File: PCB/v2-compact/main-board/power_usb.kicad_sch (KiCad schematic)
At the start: 0 parts

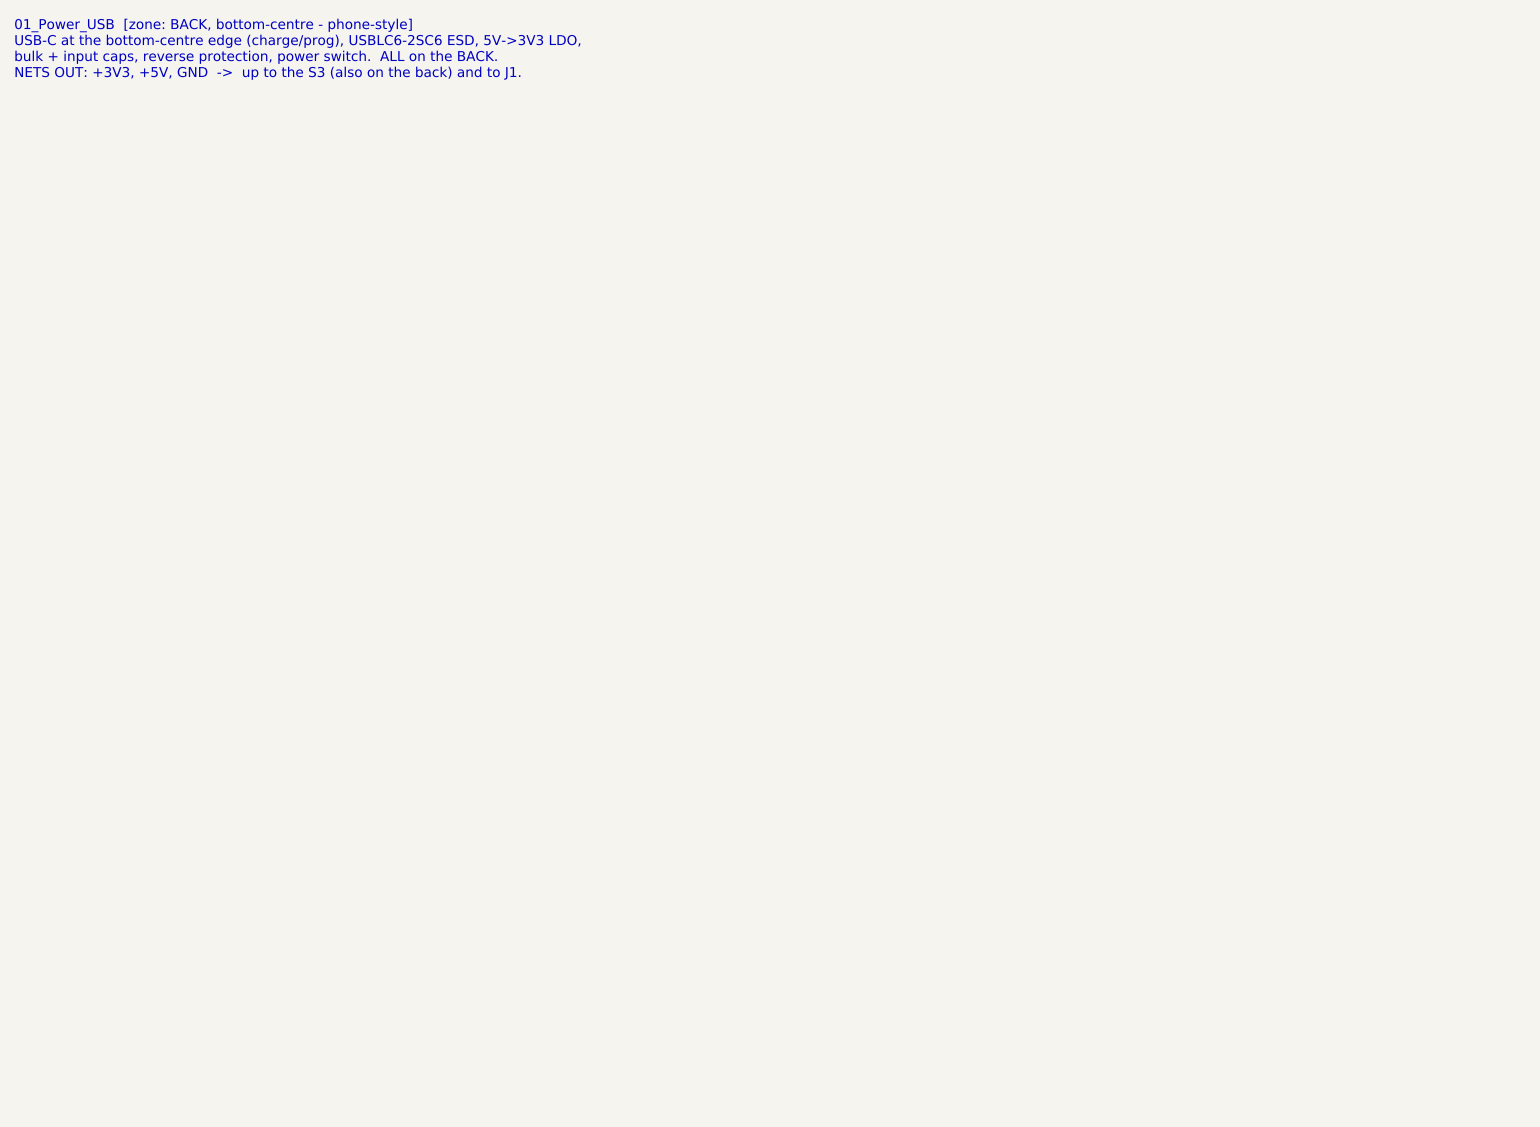
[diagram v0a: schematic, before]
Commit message: Schematics: capture PN532, GPS, IR, and both power sheets
- 07_NFC_PN532: I2C mode (I0/I1 set), 27.12MHz crystal, VMID cap, internal
  DVDD/SVDD regulator outputs correctly decoupled (not tied to 3V3), pull-ups;
  antenna pins flagged for the RF matching pass.
- 10_GPS: NEO-M9N UART to the C5, power + decoupling; bias-tee/antenna flagged.
- 11_IR: TSOP receiver + IR-LED transmitter (NPN driver).
- 02_Power (shield): local AP7361C LDO for the C5 rail + bulk caps + PWR_FLAGs.
- 01_Power_USB (main): USB-C, CC resistors, USBLC6 ESD, AP7361C 3V3 LDO.

All netlist-verified. Remaining ERC items are expected WIP (no-connects on unused
IC pins + power flags), to be cleaned once the MCU sheets tie in the shared nets.
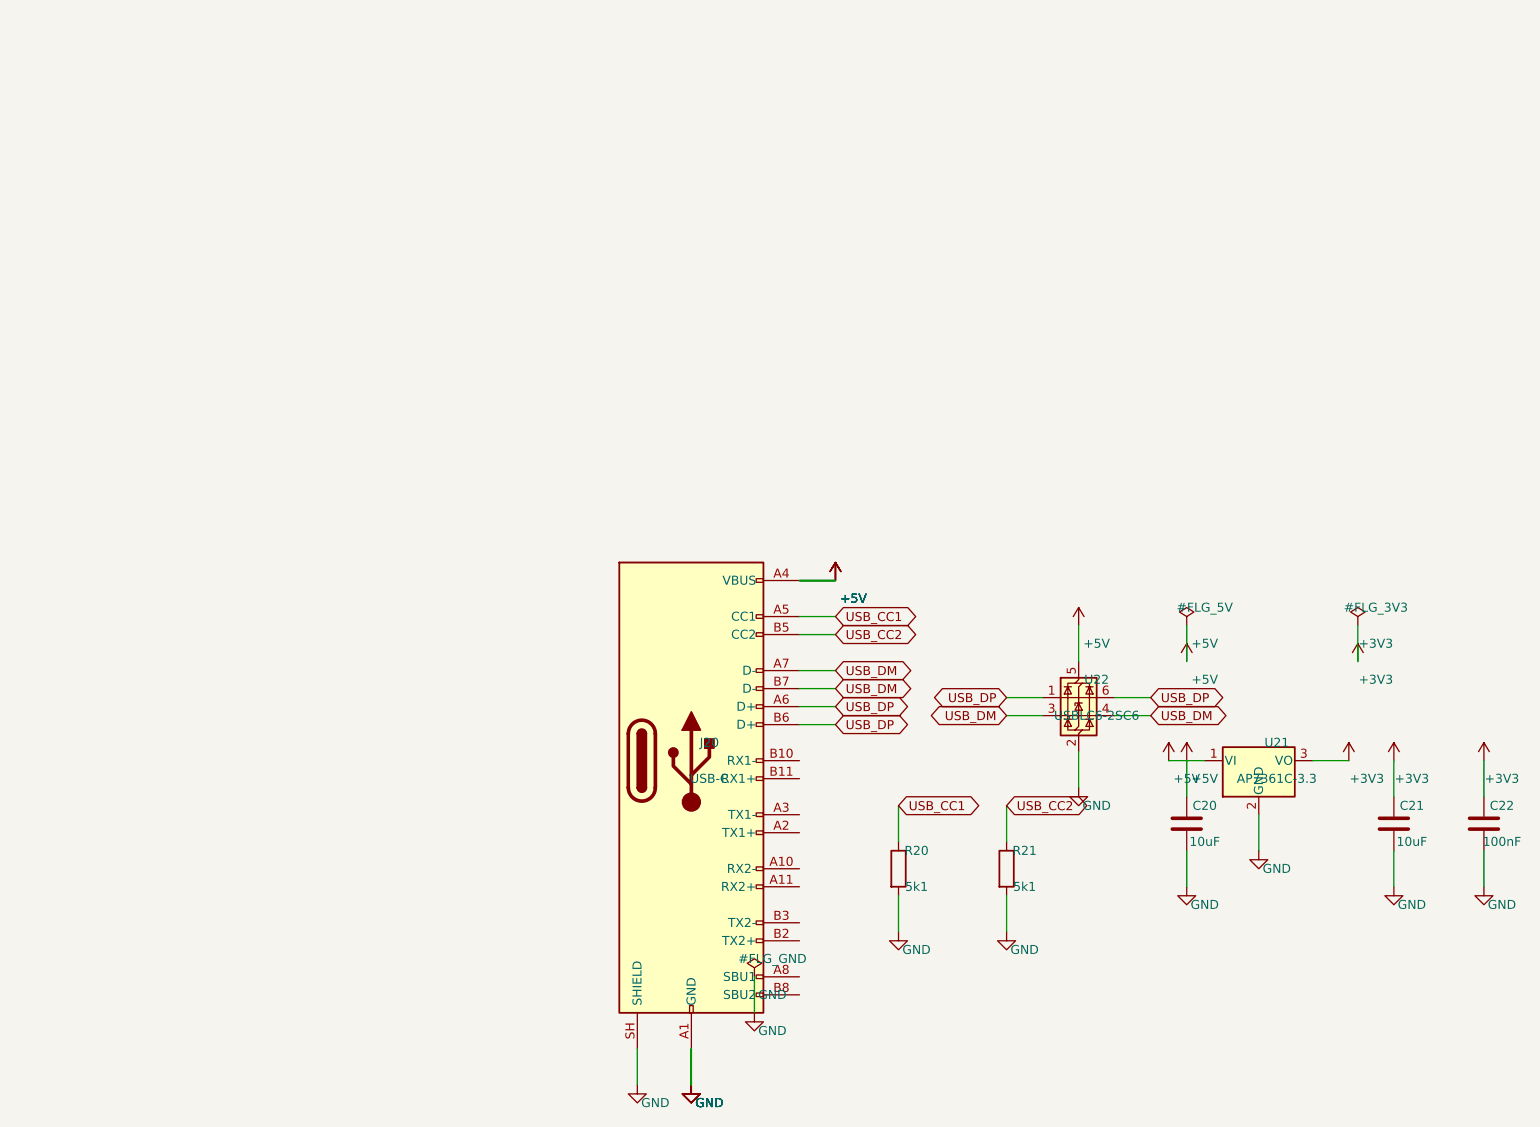
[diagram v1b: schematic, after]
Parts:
- added C20, C21: 10uF, Capacitor_SMD:C_0402_1005Metric, symbol Device:C
- added C22: 100nF, Capacitor_SMD:C_0402_1005Metric, symbol Device:C
- added J20: USB-C, Connector_USB:USB_C_Receptacle_HRO_TYPE-C-31-M-12, symbol Connector:USB_C_Receptacle
- added R20, R21: 5k1, Resistor_SMD:R_0402_1005Metric, symbol Device:R
- added U21: AP7361C-3.3, Package_TO_SOT_SMD:SOT-23-5, symbol Regulator_Linear:AP7361C-33E
- added U22: USBLC6-2SC6, Package_TO_SOT_SMD:SOT-23-6, symbol Power_Protection:USBLC6-2P6
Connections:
- new net +3V3: C21.1, C22.1, U21.3 (VO)
- new net +5V: C20.1, J20.A4 (VBUS), J20.A9 (VBUS), J20.B4 (VBUS), J20.B9 (VBUS), U21.1 (VI), U22.5 (VBUS)
- new net GND: C20.2, C21.2, C22.2, J20.A1 (GND), J20.A12 (GND), J20.B1 (GND), J20.B12 (GND), J20.SH (SHIELD), R20.2, R21.2, U21.2 (GND), U22.2 (GND)
- new net USB_CC1: J20.A5 (CC1), R20.1
- new net USB_CC2: J20.B5 (CC2), R21.1
- new net USB_DM: J20.A7 (D-), J20.B7 (D-), U22.3 (I/O2), U22.4 (I/O2)
- new net USB_DP: J20.A6 (D+), J20.B6 (D+), U22.1 (I/O1), U22.6 (I/O1)
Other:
- note removed: "01_Power_USB [zone: BACK, bottom-centre - phone-style] USB-C at the bottom-centre edge (charge/prog), USBLC6-2SC6 ESD, 5V->3V3 LDO, bulk + input caps, reverse protection, power switch. ALL on the BACK. NETS OUT: +3V3, +5V, GND -> up to the S3 (also on the back) and to J1."
